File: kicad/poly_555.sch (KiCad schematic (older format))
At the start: 34 parts, among them U21 L7805, U22 LM386

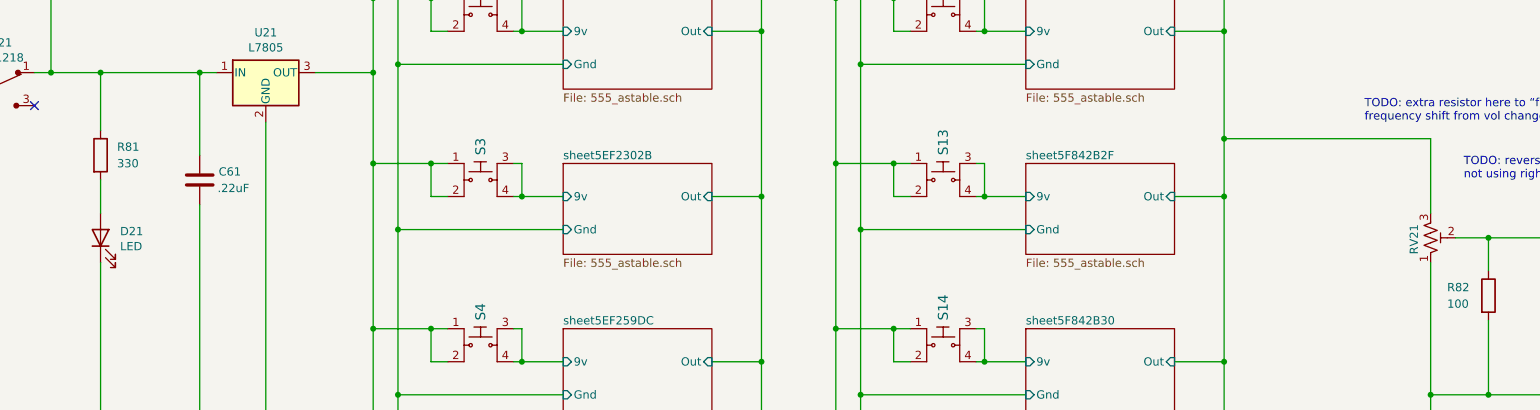
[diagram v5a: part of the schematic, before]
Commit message: Update PCB and schematic
* Finalize timing R to 100
* Drop LED ohms to 220
* Add missing 1k value to RV21
* Fix timing cap and 7805 label placements
* Widen speaker and battery relief holes
* Re-label SPK and BAT
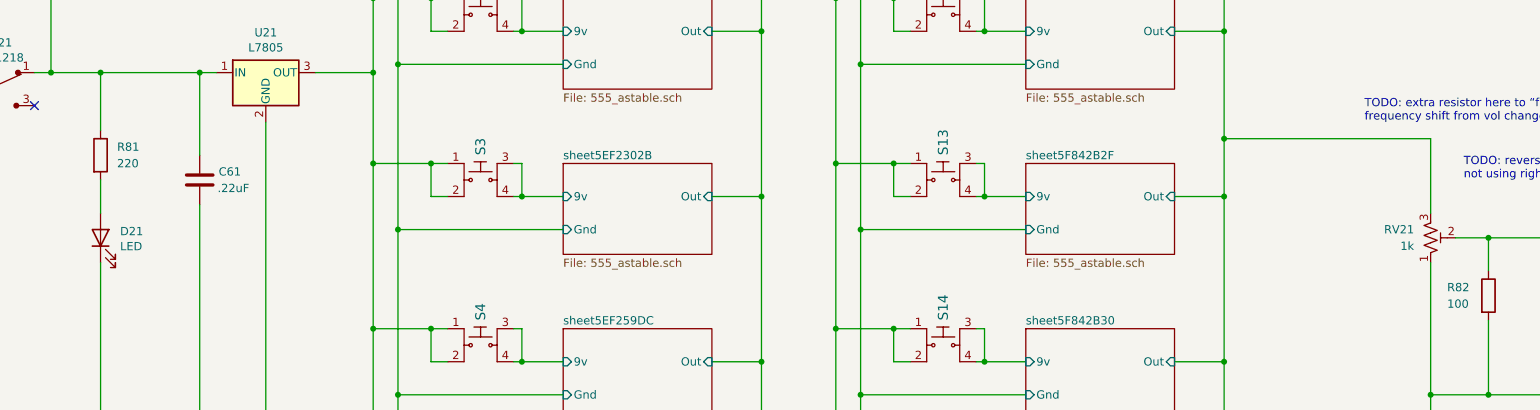
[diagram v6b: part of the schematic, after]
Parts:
- R81: value 330 -> 220
- RV21: value R_POT_TRIM_US -> 1k
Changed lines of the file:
@@
 AR Path="/5EF6060B/5FD21AA5" Ref="RV?"  Part="1"
 AR Path="/5EF7A07F/5FD21AA5" Ref="RV?"  Part="1"
-F 0 "RV21" V 10000 3850 50  0000 R CNN
-F 1 "R_POT_TRIM_US" H 10032 3705 50  0001 R CNN
+F 0 "RV21" H 10000 3700 50  0000 R CNN
+F 1 "1k" H 10000 3800 50  0000 R CNN
 F 2 "Potentiometer_THT:Potentiometer_Piher_PT-6-V_Vertical" H 10100 3750 50  0001 C CNN
 F 3 "~" H 10100 3750 50  0001 C CNN
@@
 AR Path="/60F96869/5FD21A9E" Ref="R?"  Part="1"
 F 0 "R81" H 2150 3300 50  0000 L CNN
-F 1 "330" H 2150 3200 50  0000 L CNN
+F 1 "220" H 2150 3200 50  0000 L CNN
 F 2 "Resistor_THT:R_Axial_DIN0207_L6.3mm_D2.5mm_P2.54mm_Vertical" V 1980 3250 50  0001 C CNN
 F 3 "~" H 2050 3250 50  0001 C CNN

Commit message: Tidy schematic
* Remove vestigial comments
* Fix odd 555 sheet name
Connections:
- net 555_astable/9v renamed Sheet60F4E92A/9v
- net 555_astable/Out renamed Sheet60F4E92A/Out
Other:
- note removed: "Optional “fake log” resistor\nhttps://sound-au.com/project01.htm"
- note removed: "TODO: extra resistor here to “fix”\nfrequency shift from vol change?"
- note removed: "TODO: reverse vol pot if\nnot using right trimwheel"
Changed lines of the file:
@@
 S 4850 1300 900  550
 U 60F4E92A
-F0 "555_astable" 50
+F0 "Sheet60F4E92A" 50
 F1 "555_astable.sch" 50
 F2 "Out" I R 5750 1500 50
@@
 Wire Wire Line
 	10100 3900 10100 4700
-Text Notes 9700 3050 0    50   ~ 0
-TODO: extra resistor here to “fix”\nfrequency shift from vol change?
-Text Notes 10200 5000 0    50   ~ 0
-Optional “fake log” resistor\nhttps://sound-au.com/project01.htm
-Text Notes 10300 3400 0    50   ~ 0
-TODO: reverse vol pot if\nnot using right trimwheel
 Wire Wire Line
 	10450 3750 11650 3750
